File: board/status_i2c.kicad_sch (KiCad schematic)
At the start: 44 parts, among them J5 I2C, Q10 BC548, Q11 BC548, Q12 BC548, Q13 BC548, Q14 BC548, Q7 BC548, Q8 BC548, Q9 BC548, SW11 I2C_VCC, SW12 I2C_ADDR, U10 BOB-12009, U11 MCP23008-xP, U12 CAT24C256, U13 MCP7940N-xP, U9 24LC1025, Y1 32.768kHz

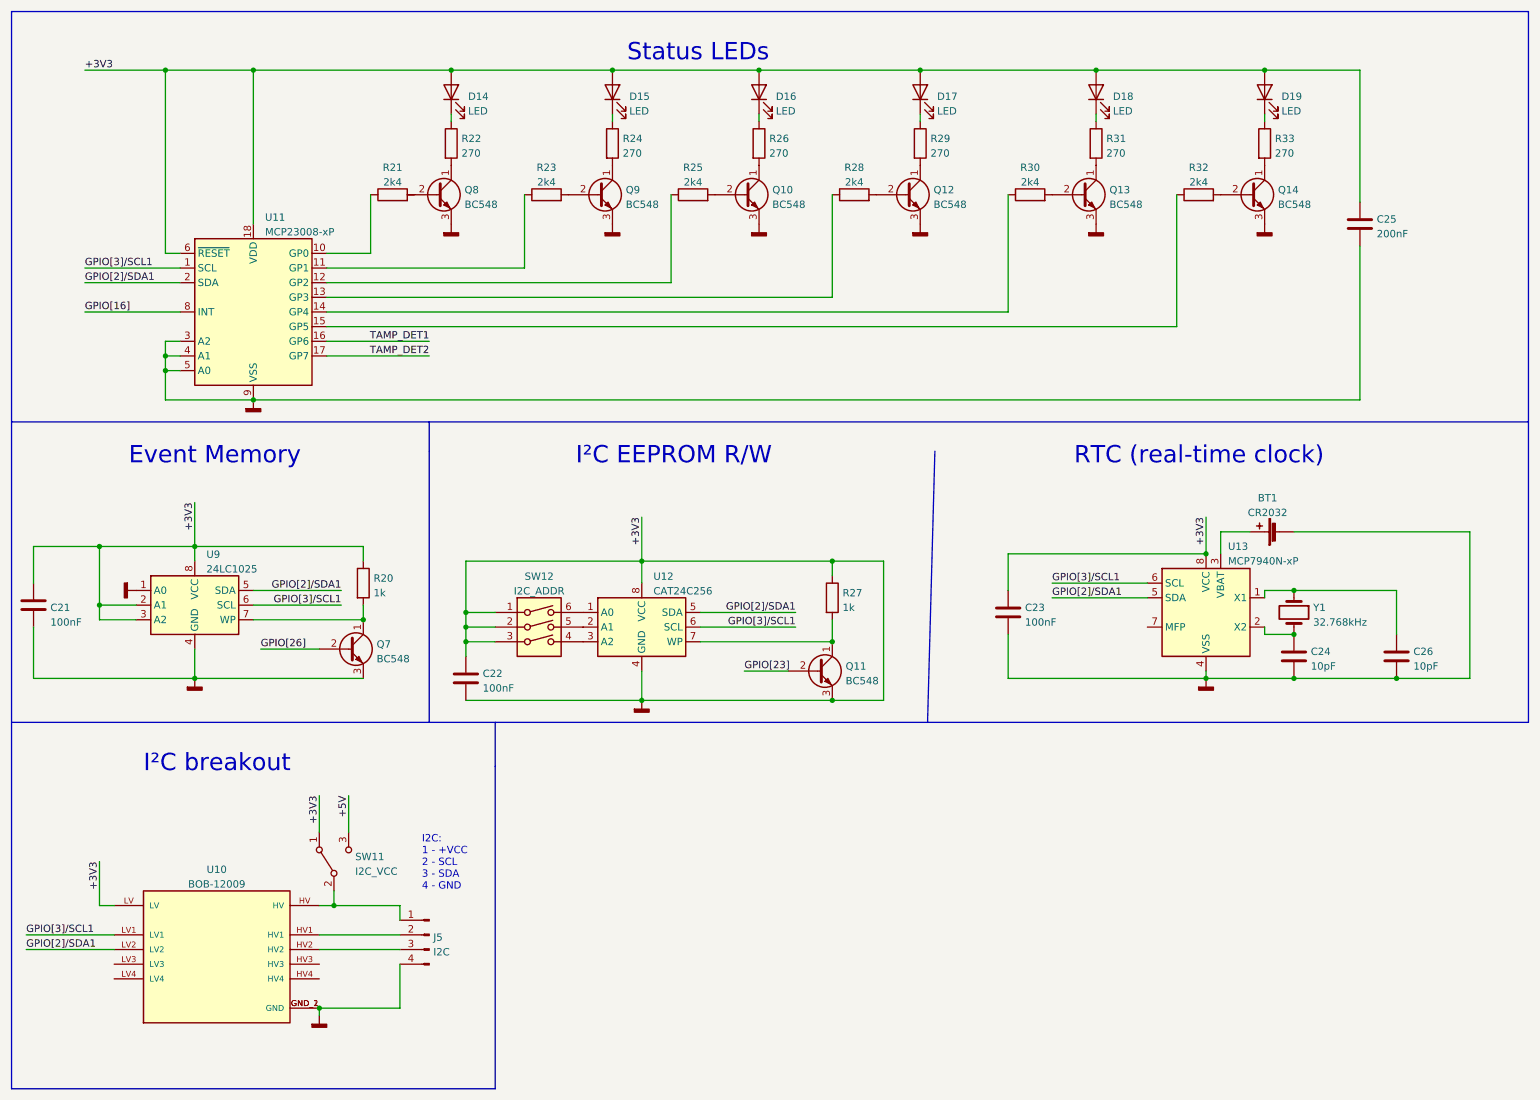
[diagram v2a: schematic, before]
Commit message: Change net descriptors.
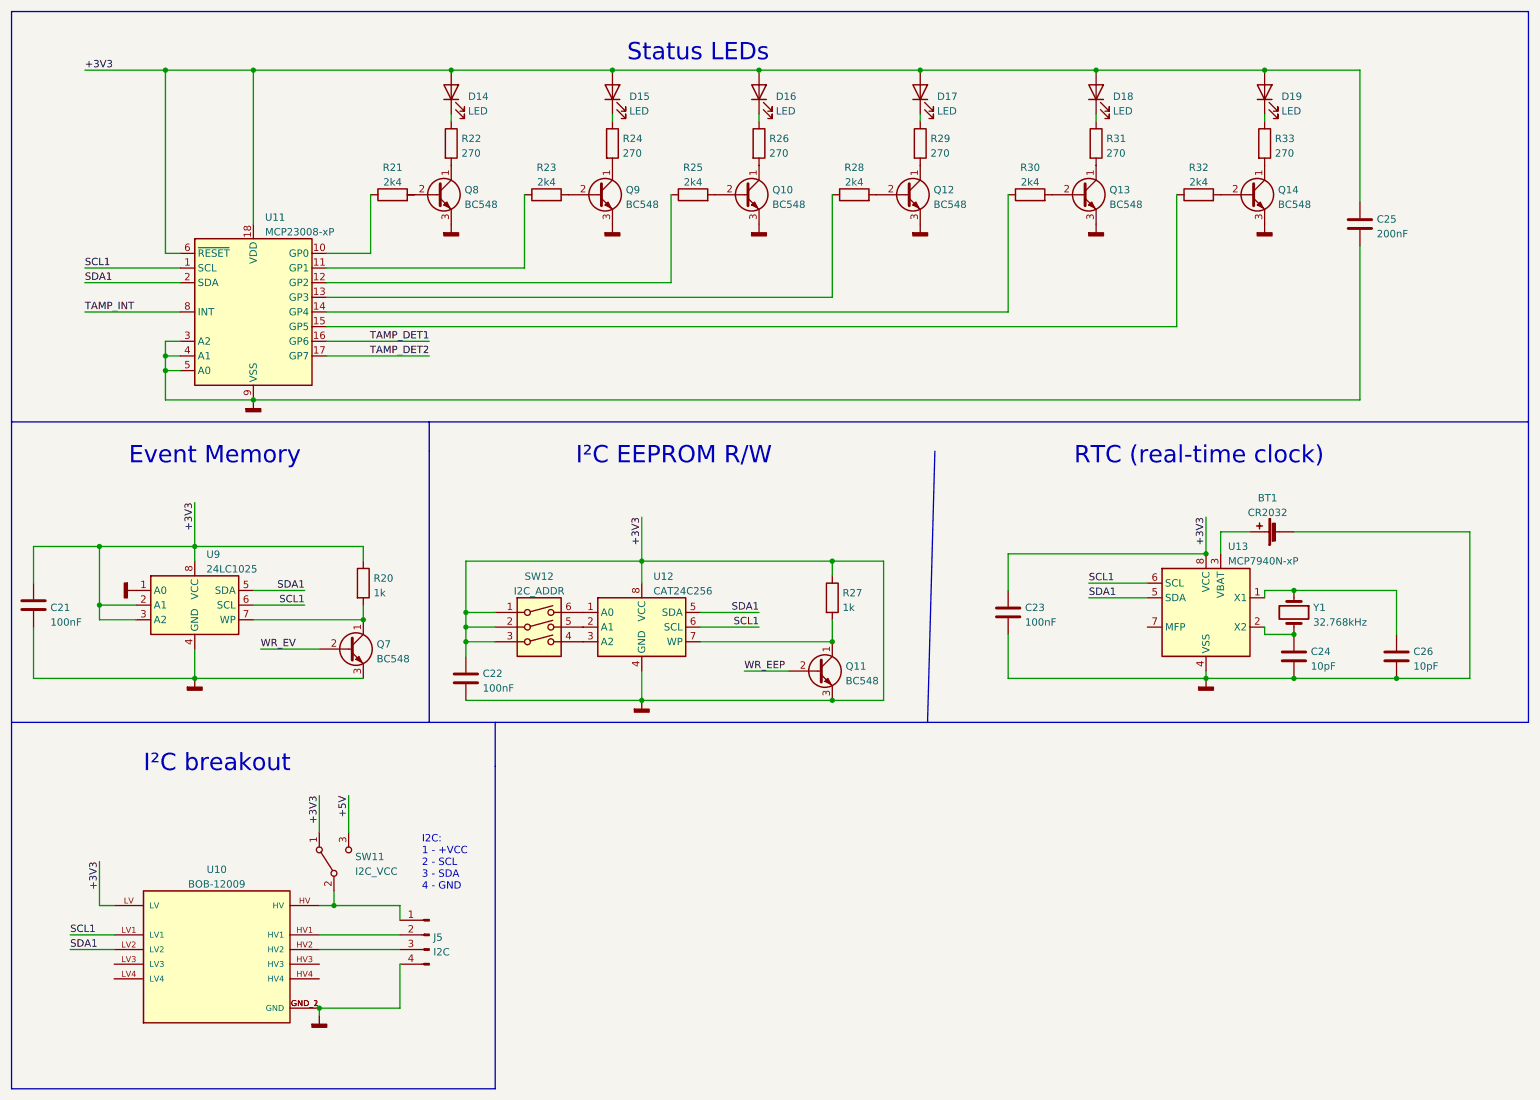
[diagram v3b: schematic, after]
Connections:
- net GPIO[16] renamed TAMP_INT
- net GPIO[23] renamed WR_EEP
- net GPIO[26] renamed WR_EV
- net GPIO[2]/SDA1 renamed SDA1
- net GPIO[3]/SCL1 renamed SCL1
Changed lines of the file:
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@@
   (junction (at 156.21 107.95) (diameter 0) (color 0 0 0 0)
   )
-  (wire (pts (xy 194.31 111.76) (xy 210.82 111.76))
+  (wire (pts (xy 200.66 111.76) (xy 210.82 111.76))
     (stroke (width 0) (type default) (color 0 0 0 0))
   )
@@
     (stroke (width 0) (type default) (color 0 0 0 0))
   )
-  (wire (pts (xy 133.35 116.84) (xy 149.86 116.84))
+  (wire (pts (xy 133.35 116.84) (xy 143.51 116.84))
     (stroke (width 0) (type default) (color 0 0 0 0))
   )
@@
     (stroke (width 0) (type default) (color 0 0 0 0))
   )
-  (wire (pts (xy 194.31 114.3) (xy 210.82 114.3))
+  (wire (pts (xy 200.66 114.3) (xy 210.82 114.3))
     (stroke (width 0) (type default) (color 0 0 0 0))
   )
@@
     (stroke (width 0) (type default) (color 0 0 0 0))
   )
-  (wire (pts (xy 55.88 115.57) (xy 71.12 115.57))
+  (wire (pts (xy 55.88 115.57) (xy 64.77 115.57))
     (stroke (width 0) (type default) (color 0 0 0 0))
   )
@@
     (stroke (width 0) (type default) (color 0 0 0 0))
   )
-  (wire (pts (xy 133.35 119.38) (xy 149.86 119.38))
+  (wire (pts (xy 133.35 119.38) (xy 143.51 119.38))
     (stroke (width 0) (type default) (color 0 0 0 0))
   )
@@
     (stroke (width 0) (type default) (color 0 0 0 0))
   )
-  (wire (pts (xy 55.88 113.03) (xy 71.12 113.03))
+  (wire (pts (xy 55.88 113.03) (xy 64.77 113.03))
     (stroke (width 0) (type default) (color 0 0 0 0))
   )
@@
     (stroke (width 0) (type default) (color 0 0 0 0))
   )
-  (wire (pts (xy 16.51 172.72) (xy 31.75 172.72))
+  (wire (pts (xy 24.13 172.72) (xy 31.75 172.72))
     (stroke (width 0) (type default) (color 0 0 0 0))
   )
@@
     (stroke (width 0) (type default) (color 0 0 0 0))
   )
-  (wire (pts (xy 16.51 175.26) (xy 31.75 175.26))
+  (wire (pts (xy 24.13 175.26) (xy 31.75 175.26))
     (stroke (width 0) (type default) (color 0 0 0 0))
   )
@@
     (effects (font (size 3 3)) (justify left bottom))
   )
-  (label "GPIO[2]{slash}SDA1" (at 71.12 113.03 180)
-    (effects (font (size 1.27 1.27)) (justify right bottom))
-  )
   (label "+3V3" (at 29.21 160.02 270)
     (effects (font (size 1.27 1.27)) (justify right bottom))
   )
-  (label "GPIO[3]{slash}SCL1" (at 149.86 119.38 180)
-    (effects (font (size 1.27 1.27)) (justify right bottom))
-  )
-  (label "GPIO[2]{slash}SDA1" (at 26.67 59.69 0)
-    (effects (font (size 1.27 1.27)) (justify left bottom))
-  )
-  (label "GPIO[2]{slash}SDA1" (at 194.31 114.3 0)
-    (effects (font (size 1.27 1.27)) (justify left bottom))
-  )
-  (label "GPIO[26]" (at 57.15 123.19 0)
-    (effects (font (size 1.27 1.27)) (justify left bottom))
-  )
-  (label "GPIO[2]{slash}SDA1" (at 149.86 116.84 180)
-    (effects (font (size 1.27 1.27)) (justify right bottom))
+  (label "SDA1" (at 200.66 114.3 0)
+    (effects (font (size 1.27 1.27)) (justify left bottom))
+  )
+  (label "SDA1" (at 26.67 59.69 0)
+    (effects (font (size 1.27 1.27)) (justify left bottom))
+  )
+  (label "SDA1" (at 64.77 113.03 180)
+    (effects (font (size 1.27 1.27)) (justify right bottom))
+  )
+  (label "SDA1" (at 143.51 116.84 180)
+    (effects (font (size 1.27 1.27)) (justify right bottom))
+  )
+  (label "WR_EV" (at 57.15 123.19 0)
+    (effects (font (size 1.27 1.27)) (justify left bottom))
   )
   (label "TAMP_DET1" (at 86.36 69.85 180)
     (effects (font (size 1.27 1.27)) (justify right bottom))
   )
-  (label "GPIO[16]" (at 26.67 64.77 0)
-    (effects (font (size 1.27 1.27)) (justify left bottom))
-  )
-  (label "GPIO[3]{slash}SCL1" (at 71.12 115.57 180)
-    (effects (font (size 1.27 1.27)) (justify right bottom))
+  (label "TAMP_INT" (at 26.67 64.77 0)
+    (effects (font (size 1.27 1.27)) (justify left bottom))
+  )
+  (label "SCL1" (at 64.77 115.57 180)
+    (effects (font (size 1.27 1.27)) (justify right bottom))
+  )
+  (label "SCL1" (at 26.67 57.15 0)
+    (effects (font (size 1.27 1.27)) (justify left bottom))
   )
   (label "TAMP_DET2" (at 86.36 72.39 180)
     (effects (font (size 1.27 1.27)) (justify right bottom))
   )
+  (label "SCL1" (at 200.66 111.76 0)
+    (effects (font (size 1.27 1.27)) (justify left bottom))
+  )
   (label "+3V3" (at 26.67 22.86 0)
     (effects (font (size 1.27 1.27)) (justify left bottom))
@@
     (effects (font (size 1.27 1.27)) (justify right bottom))
   )
-  (label "GPIO[2]{slash}SDA1" (at 16.51 175.26 0)
+  (label "SCL1" (at 24.13 172.72 0)
     (effects (font (size 1.27 1.27)) (justify left bottom))
   )
@@
     (effects (font (size 1.27 1.27)) (justify right bottom))
   )
+  (label "SCL1" (at 143.51 119.38 180)
+    (effects (font (size 1.27 1.27)) (justify right bottom))
+  )
   (label "+5V" (at 72.39 148.59 270)
     (effects (font (size 1.27 1.27)) (justify right bottom))
   )
-  (label "GPIO[3]{slash}SCL1" (at 26.67 57.15 0)
-    (effects (font (size 1.27 1.27)) (justify left bottom))
-  )
-  (label "GPIO[23]" (at 140.97 127 0)
-    (effects (font (size 1.27 1.27)) (justify left bottom))
-  )
-  (label "GPIO[3]{slash}SCL1" (at 16.51 172.72 0)
-    (effects (font (size 1.27 1.27)) (justify left bottom))
-  )
-  (label "GPIO[3]{slash}SCL1" (at 194.31 111.76 0)
-    (effects (font (size 1.27 1.27)) (justify left bottom))
-  )
+  (label "SDA1" (at 24.13 175.26 0)
+    (effects (font (size 1.27 1.27)) (justify left bottom))
+  )
+  (label "WR_EEP" (at 140.97 127 0)
+    (effects (font (size 1.27 1.27)) (justify left bottom))
+  )

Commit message: Make it a multiboard project.
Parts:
- added Q13, Q14, Q17, Q18: BC548, Package_TO_SOT_THT:TO-92_Inline, symbol Transistor_BJT:BC548
- added R30, R31, R36, R37: 2k4, Resistor_THT:R_Axial_DIN0516_L15.5mm_D5.0mm_P7.62mm_Vertical, symbol Device:R
- added SW5: TD_B, Connector_Wire:SolderWire-1sqmm_1x02_P5.4mm_D1.4mm_OD2.7mm, symbol Switch:SW_Push_Open
- added SW6: TD_A, Connector_Wire:SolderWire-1sqmm_1x02_P5.4mm_D1.4mm_OD2.7mm, symbol Switch:SW_Push_Open
- added SW7: TD2_B, Connector_Wire:SolderWire-1sqmm_1x02_P5.4mm_D1.4mm_OD2.7mm, symbol Switch:SW_Push
- added SW8: TD2_A, Connector_Wire:SolderWire-1sqmm_1x02_P5.4mm_D1.4mm_OD2.7mm, symbol Switch:SW_Push
- BT1: footprint Battery:BatteryHolder_Keystone_1058_1x2032 -> Battery:Battery_Panasonic_CR2032-VS1N_Vertical_CircularHoles
- renumbered C21 to C20, C22 to C21, C23 to C22, C24 to C23, C25 to C24, C26 to C25, J5 to J12, Q13 to Q15, Q14 to Q16, R30 to R32, R31 to R33, R32 to R34, R33 to R35, SW11 to SW3, SW12 to SW4, U12 to U10, U13 to U11, U9 to U7, U10 to U8, U11 to U9
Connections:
- net GNDD: no longer BT1.2 (-), C20.1, C20.2, C21.1, C21.2, C22.1, C22.2, C23.2, C24.1, C24.2, C25.2, D14.2 (A), D15.2 (A), D16.2 (A), D17.2 (A), D18.2 (A), D19.2 (A), J12.4 (Pin_4), Q11.3 (E), Q7.3 (E), R20.1, R27.1, SW3.1 (A), SW4.1, SW4.2, SW4.3, U10.4 (GND), U10.8 (VCC), U11.4 (VSS), U11.8 (VCC), U7.2 (A1), U7.3 (A2), U7.4 (GND), U7.8 (VCC), U8.GND_1 (GND), U8.GND_2 (GND), U8.LV, U9.18 (VDD), U9.3 (A2), U9.4 (A1), U9.5 (A0), U9.6 (~{RESET}), U9.9 (VSS)
- net TAMP_DET1: now also Q13.3 (E), Q14.3 (E)
- net TAMP_DET2: now also Q17.1 (C)
- net at Q8.2 (B): now also R21.2
- new net: Q17.3 (E), Q18.1 (C)
- new net: Q18.2 (B), R37.2
- new net: BT1.2 (-), C22.2, C23.2, C25.2, U11.4 (VSS)
- new net: R30.1, SW5.1 (A)
- new net: Q17.2 (B), R36.2
- new net: Q14.2 (B), R31.2
- new net: R31.1, SW6.1 (A)
- new net: R37.1, SW8.1
- new net: R36.1, SW7.1
- new net: Q13.2 (B), R30.2
- new net +3V3: C20.1, C20.2, C21.1, C21.2, C22.1, C24.1, C24.2, D14.2 (A), D15.2 (A), D16.2 (A), D17.2 (A), D18.2 (A), D19.2 (A), J12.4 (Pin_4), Q11.3 (E), Q13.1 (C), Q14.1 (C), Q18.3 (E), Q7.3 (E), R20.1, R27.1, SW3.1 (A), SW4.1, SW4.2, SW4.3, SW5.2 (B), SW6.2 (B), SW7.2, SW8.2, U10.4 (GND), U10.8 (VCC), U11.8 (VCC), U7.2 (A1), U7.3 (A2), U7.4 (GND), U7.8 (VCC), U8.GND_1 (GND), U8.GND_2 (GND), U8.LV, U9.18 (VDD), U9.3 (A2), U9.4 (A1), U9.5 (A0), U9.6 (~{RESET}), U9.9 (VSS)
- no-connect marks 0 -> 5
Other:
- note added: "Tamper detection"
- moved on the sheet: BT1, C21, Q11, R21, R27, SW4, U10

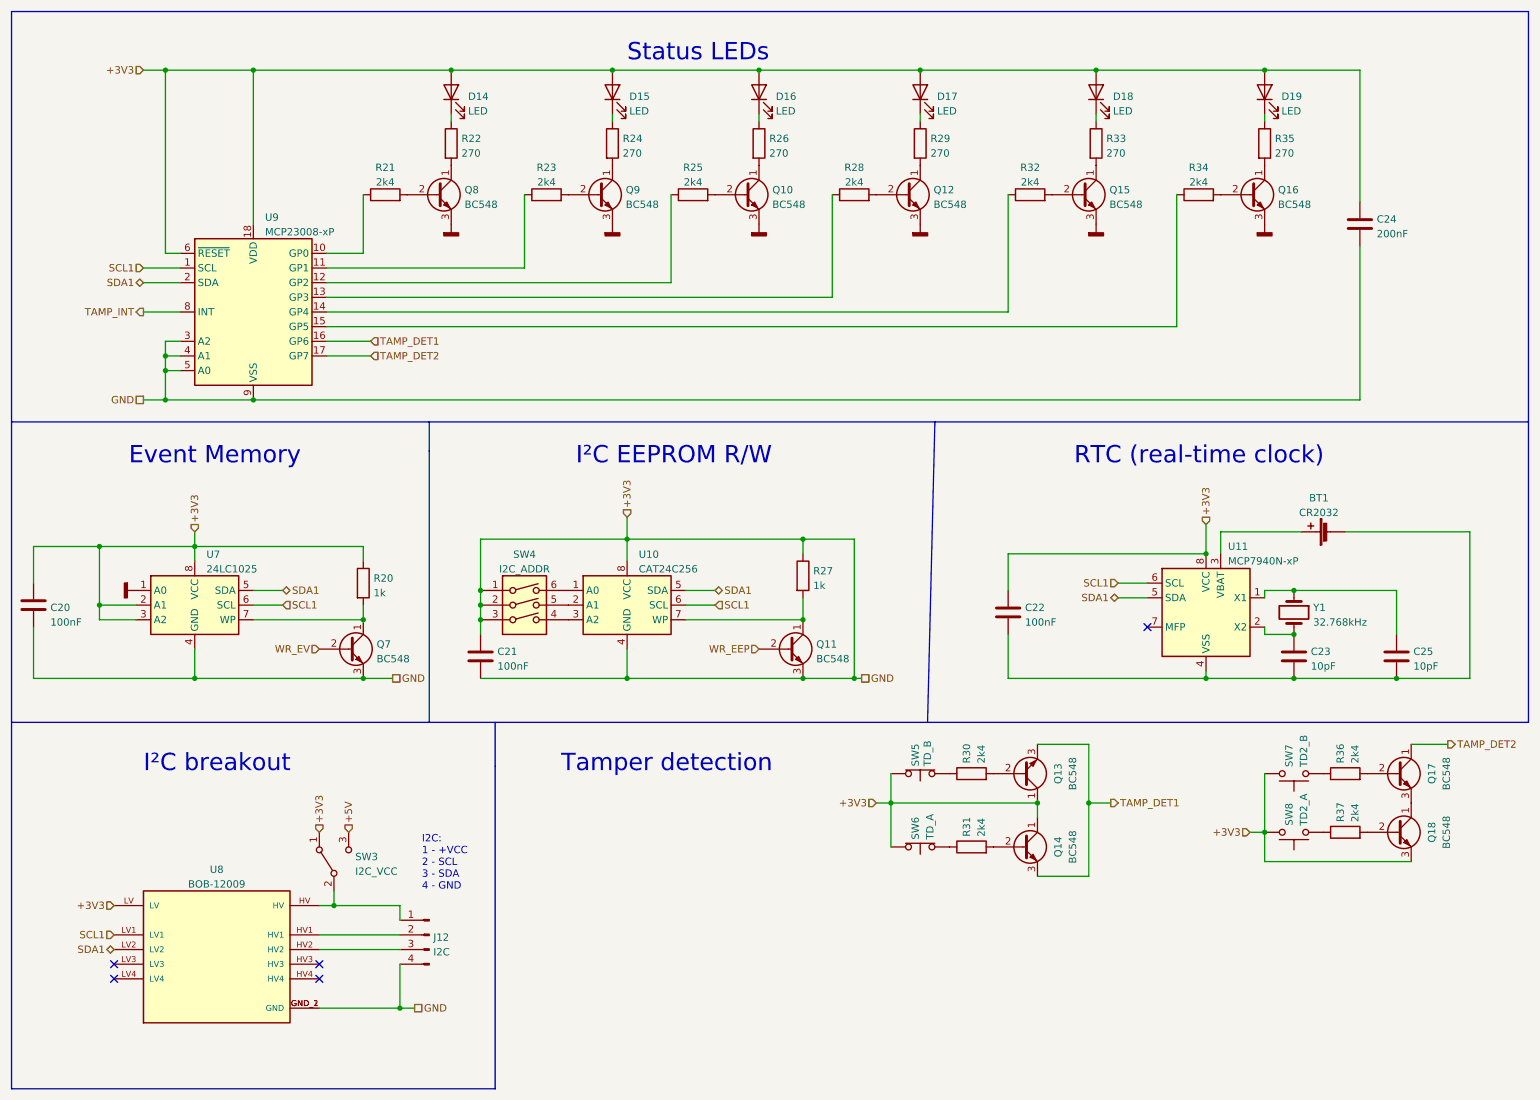
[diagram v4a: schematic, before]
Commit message: Modularize board.
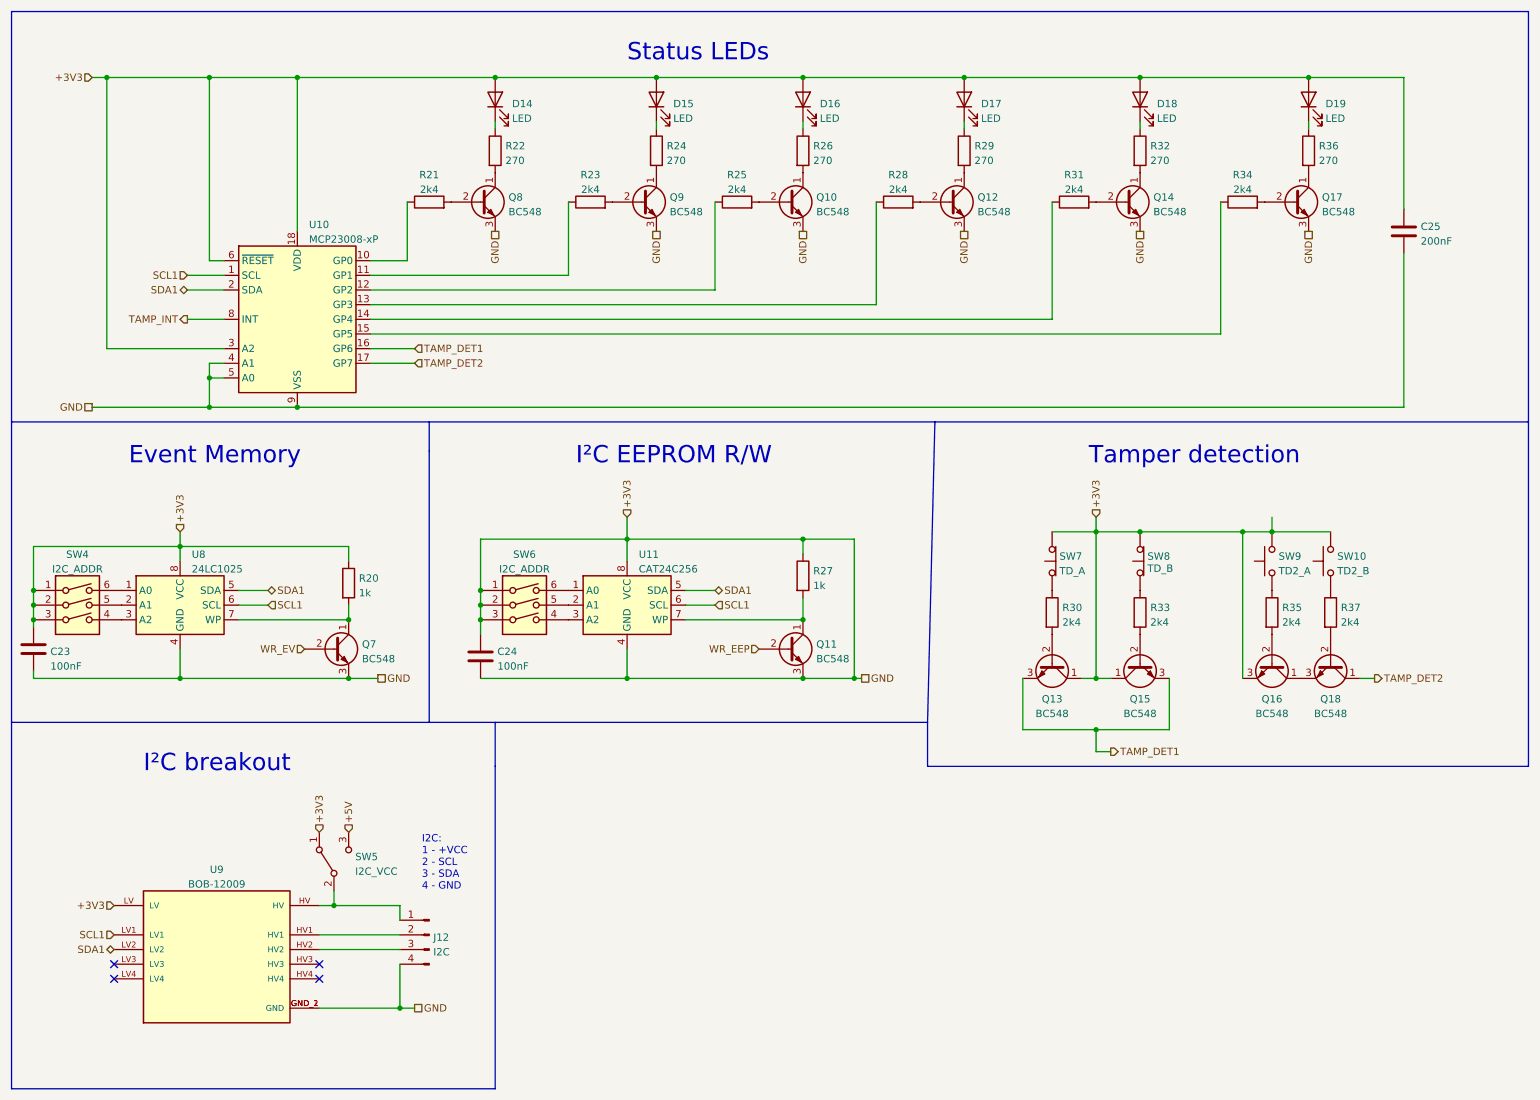
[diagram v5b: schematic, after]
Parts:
- removed BT1: CR2032, Battery:Battery_Panasonic_CR2032-VS1N_Vertical_CircularHoles, symbol Device:Battery_Cell
- removed C22: 100nF, Capacitor_THT:C_Disc_D5.0mm_W2.5mm_P5.00mm, symbol Device:C
- removed C23, C25: 10pF, Capacitor_THT:C_Radial_D6.3mm_H5.0mm_P2.50mm, symbol Device:C
- removed U11: MCP7940N-xP, Package_DIP:DIP-8_W7.62mm_Socket_LongPads, symbol Timer_RTC:MCP7940N-xP
- removed Y1: 32.768kHz, Crystal:Crystal_C26-LF_D2.1mm_L6.5mm_Vertical, symbol Device:Crystal
- added SW4: I2C_ADDR, Button_Switch_THT:SW_DIP_SPSTx03_Slide_9.78x9.8mm_W7.62mm_P2.54mm, symbol Switch:SW_DIP_x03
- renumbered C20 to C23, C21 to C24, C24 to C25, Q14 to Q13, Q15 to Q14, Q13 to Q15, Q18 to Q16, Q16 to Q17, Q17 to Q18, R31 to R30, R32 to R31, R33 to R32, R30 to R33, R37 to R35, R35 to R36, R36 to R37, SW7 to SW10, SW3 to SW5, SW4 to SW6, SW6 to SW7, SW5 to SW8, SW8 to SW9, U9 to U10, U10 to U11, U7 to U8, U8 to U9
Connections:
- net +3V3: now also Q10.3 (E), Q12.3 (E), Q14.3 (E), Q17.3 (E), Q8.3 (E), Q9.3 (E), SW4.1, SW4.2, SW4.3; no longer U8.2 (A1), U8.3 (A2)
- removed net GNDD: Q10.3 (E), Q12.3 (E), Q14.3 (E), Q17.3 (E), Q8.3 (E), Q9.3 (E), U8.1 (A0)
- new net: SW4.6, U8.1 (A0)
- new net: SW4.5, U8.2 (A1)
- new net: SW4.4, U8.3 (A2)
- no-connect marks 5 -> 4
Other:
- note removed: "RTC (real-time clock)"
- moved on the sheet: C23, C25, D14, D15, D16, D17, D18, D19, Q10, Q12, Q13, Q14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
